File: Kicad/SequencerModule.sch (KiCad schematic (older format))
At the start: 0 parts

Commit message: added symbols on schematics
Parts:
- added A1: Arduino_Nano_v3.x, Module:Arduino_Nano, symbol MCU_Module:Arduino_Nano_v3.x
- added C1: 0.1μF, symbol Device:C_Small
- added C2, C3: 10uF, symbol Device:CP1_Small
- added C4: 0.1uF, symbol Device:C_Small
- added D1, D4: LED, symbol Device:LED
- added D2, D3: D_Small, symbol Device:D_Small
- added J1, J2, J3, J4, J5, J6, J7: TRIG_OUT, Connector_Audio:Jack_3.5mm_QingPu_WQP-PJ398SM_Vertical_CircularHoles, symbol Connector:AudioJack2_SwitchT
- added JP1: EURO_PWR_2x5, symbol eurorack_custom:urorack_EURO_PWR_2x5
- added L1, L2: L_Small, symbol Device:L_Small
- added Q1, Q2: 2N3904, Package_TO_SOT_THT:TO-92_Inline, symbol Transistor_BJT:2N3904
- added R1, R5: 1k, symbol Device:R
- added R2, R6: R1k, symbol Device:R
- added R3, R7: 1k8, symbol Device:R
- added R4, R8: 120, symbol Device:R
- added U1: L78L05_SOT89, Package_TO_SOT_SMD:SOT-89-3, symbol Regulator_Linear:L78L05_SOT89
- added U2: MCP4822, symbol Analog_DAC:MCP4822
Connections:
- net labels added: +12V, +5V, -12V, CS, DAC_CV1, DAC_CV2, GND, MCU_TRIG_OUT_1, MCU_TRIG_OUT_2, SCLK, SDI
- wire segments 0 -> 81

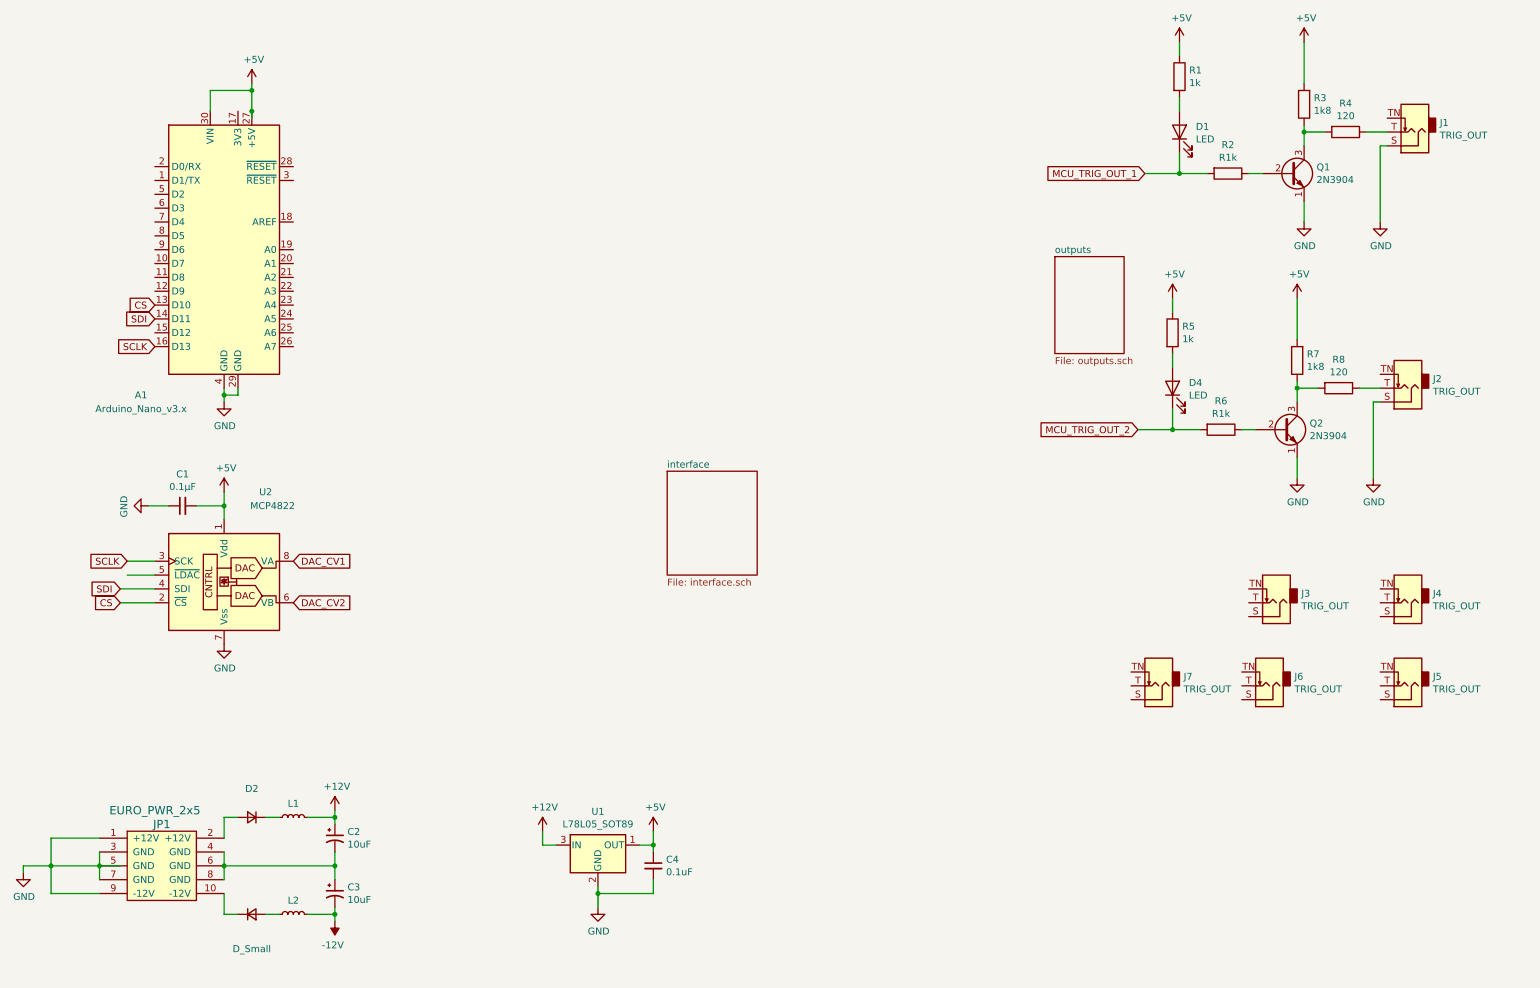
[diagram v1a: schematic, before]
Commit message: added CV output buffers
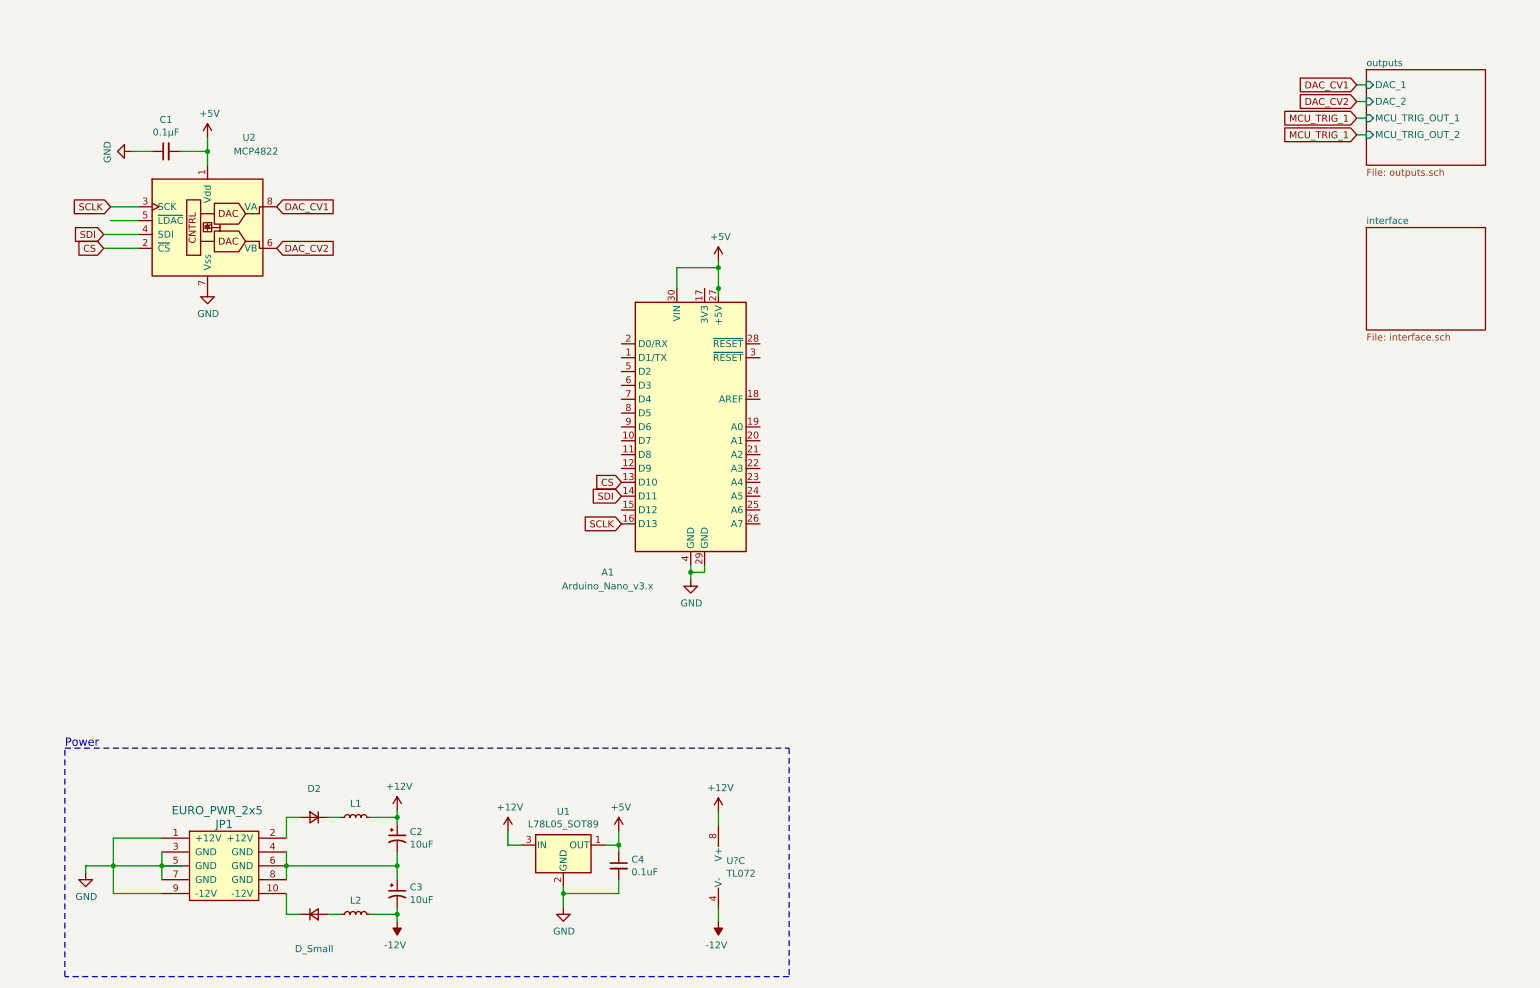
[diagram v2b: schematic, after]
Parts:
- removed D1, D4: LED, symbol Device:LED
- removed J1, J2, J3, J4, J5, J6, J7: TRIG_OUT, Connector_Audio:Jack_3.5mm_QingPu_WQP-PJ398SM_Vertical_CircularHoles, symbol Connector:AudioJack2_SwitchT
- removed Q1, Q2: 2N3904, Package_TO_SOT_THT:TO-92_Inline, symbol Transistor_BJT:2N3904
- removed R1, R5: 1k, symbol Device:R
- removed R2, R6: R1k, symbol Device:R
- removed R3, R7: 1k8, symbol Device:R
- removed R4, R8: 120, symbol Device:R
- added U?: TL072, symbol Amplifier_Operational:TL072
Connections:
- net labels added: MCU_TRIG_1
- net labels removed: MCU_TRIG_OUT_1, MCU_TRIG_OUT_2
- wire segments 81 -> 59
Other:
- note added: "Power"
- moved on the sheet: A1, C1, C2, C3, C4, D2, JP1, L1, L2, U1, U2

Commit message: making progress on interface
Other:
- moved on the sheet: A1, C1, U2
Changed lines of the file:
@@
 L Analog_DAC:MCP4822 U2
 U 1 1 5FAC40C6
-P 1880 2090
-F 0 "U2" H 2180 2690 50  0000 C CNN
-F 1 "MCP4822" H 2230 2590 50  0000 C CNN
-F 2 "" H 2680 1790 50  0001 C CNN
-F 3 "http://ww1.microchip.com/downloads/en/DeviceDoc/20002249B.pdf" H 2680 1790 50  0001 C CNN
-	1    1880 2090
+P 2790 2940
+F 0 "U2" H 3090 3540 50  0000 C CNN
+F 1 "MCP4822" H 3140 3440 50  0000 C CNN
+F 2 "" H 3590 2640 50  0001 C CNN
+F 3 "http://ww1.microchip.com/downloads/en/DeviceDoc/20002249B.pdf" H 3590 2640 50  0001 C CNN
+	1    2790 2940
 	1    0    0    -1
 $EndComp
@@
 L power:GND #PWR0101
 U 1 1 5FAC5967
-P 1880 2590
-F 0 "#PWR0101" H 1880 2340 50  0001 C CNN
-F 1 "GND" H 1885 2417 50  0000 C CNN
-F 2 "" H 1880 2590 50  0001 C CNN
-F 3 "" H 1880 2590 50  0001 C CNN
-	1    1880 2590
+P 2790 3440
+F 0 "#PWR0101" H 2790 3190 50  0001 C CNN
+F 1 "GND" H 2795 3267 50  0000 C CNN
+F 2 "" H 2790 3440 50  0001 C CNN
+F 3 "" H 2790 3440 50  0001 C CNN
+	1    2790 3440
 	1    0    0    -1
 $EndComp
@@
 L Device:C_Small C1
 U 1 1 5FAC8AF5
-P 1580 1590
-F 0 "C1" V 1809 1590 50  0000 C CNN
-F 1 "0.1μF" V 1718 1590 50  0000 C CNN
-F 2 "" H 1580 1590 50  0001 C CNN
-F 3 "~" H 1580 1590 50  0001 C CNN
-	1    1580 1590
+P 2490 2440
+F 0 "C1" V 2719 2440 50  0000 C CNN
+F 1 "0.1μF" V 2628 2440 50  0000 C CNN
+F 2 "" H 2490 2440 50  0001 C CNN
+F 3 "~" H 2490 2440 50  0001 C CNN
+	1    2490 2440
 	0    -1   -1   0
 $EndComp
 Wire Wire Line
-	1880 1490 1880 1590
-Wire Wire Line
-	1680 1590 1880 1590
-Connection ~ 1880 1590
-Wire Wire Line
-	1880 1590 1880 1690
+	2790 2340 2790 2440
+Wire Wire Line
+	2590 2440 2790 2440
+Connection ~ 2790 2440
+Wire Wire Line
+	2790 2440 2790 2540
 $Comp
 L power:GND #PWR0102
 U 1 1 5FAC9D1B
-P 1330 1590
-F 0 "#PWR0102" H 1330 1340 50  0001 C CNN
-F 1 "GND" H 1335 1417 50  0000 C CNN
-F 2 "" H 1330 1590 50  0001 C CNN
-F 3 "" H 1330 1590 50  0001 C CNN
-	1    1330 1590
+P 2240 2440
+F 0 "#PWR0102" H 2240 2190 50  0001 C CNN
+F 1 "GND" H 2245 2267 50  0000 C CNN
+F 2 "" H 2240 2440 50  0001 C CNN
+F 3 "" H 2240 2440 50  0001 C CNN
+	1    2240 2440
 	0    1    1    0
 $EndComp
 Wire Wire Line
-	1330 1590 1480 1590
-Text GLabel 1180 1990 0    50   Input ~ 0
+	2240 2440 2390 2440
+Text GLabel 2090 2840 0    50   Input ~ 0
 SCLK
-Text GLabel 1130 2290 0    50   Input ~ 0
+Text GLabel 2040 3140 0    50   Input ~ 0
 CS
-Text GLabel 2380 1990 2    50   Input ~ 0
+Text GLabel 3290 2840 2    50   Input ~ 0
 DAC_CV1
-Text GLabel 2380 2290 2    50   Input ~ 0
+Text GLabel 3290 3140 2    50   Input ~ 0
 DAC_CV2
 Wire Wire Line
-	1180 1990 1380 1990
-Wire Wire Line
-	1180 2090 1380 2090
-Wire Wire Line
-	1130 2190 1380 2190
-Wire Wire Line
-	1130 2290 1380 2290
+	2090 2840 2290 2840
+Wire Wire Line
+	2090 2940 2290 2940
+Wire Wire Line
+	2040 3040 2290 3040
+Wire Wire Line
+	2040 3140 2290 3140
 $Comp
 L MCU_Module:Arduino_Nano_v3.x A1
 U 1 1 5FAD0791
-P 5370 3580
-F 0 "A1" H 4770 2530 50  0000 C CNN
-F 1 "Arduino_Nano_v3.x" H 4770 2430 50  0000 C CNN
-F 2 "Module:Arduino_Nano" H 5370 3580 50  0001 C CIN
-F 3 "http://www.mouser.com/pdfdocs/Gravitech_Arduino_Nano3_0.pdf" H 5370 3580 50  0001 C CNN
-	1    5370 3580
+P 6920 3010
+F 0 "A1" H 6320 1960 50  0000 C CNN
+F 1 "Arduino_Nano_v3.x" H 6320 1860 50  0000 C CNN
+F 2 "Module:Arduino_Nano" H 6920 3010 50  0001 C CIN
+F 3 "http://www.mouser.com/pdfdocs/Gravitech_Arduino_Nano3_0.pdf" H 6920 3010 50  0001 C CNN
+	1    6920 3010
 	1    0    0    -1
 $EndComp
@@
 L power:GND #PWR0103
 U 1 1 5FAD2D29
-P 5370 4680
-F 0 "#PWR0103" H 5370 4430 50  0001 C CNN
-F 1 "GND" H 5375 4507 50  0000 C CNN
-F 2 "" H 5370 4680 50  0001 C CNN
-F 3 "" H 5370 4680 50  0001 C CNN
-	1    5370 4680
-	1    0    0    -1
-$EndComp
-Wire Wire Line
-	5370 4580 5370 4630
-Wire Wire Line
-	5470 4580 5470 4630
-Wire Wire Line
-	5470 4630 5370 4630
-Connection ~ 5370 4630
-Wire Wire Line
-	5370 4630 5370 4680
-Text GLabel 4870 4080 0    50   Input ~ 0
+P 6920 4110
+F 0 "#PWR0103" H 6920 3860 50  0001 C CNN
+F 1 "GND" H 6925 3937 50  0000 C CNN
+F 2 "" H 6920 4110 50  0001 C CNN
+F 3 "" H 6920 4110 50  0001 C CNN
+	1    6920 4110
+	1    0    0    -1
+$EndComp
+Wire Wire Line
+	6920 4010 6920 4060
+Wire Wire Line
+	7020 4010 7020 4060
+Wire Wire Line
+	7020 4060 6920 4060
+Connection ~ 6920 4060
+Wire Wire Line
+	6920 4060 6920 4110
+Text GLabel 6420 3510 0    50   Input ~ 0
 SDI
-Text GLabel 1130 2190 0    50   Input ~ 0
+Text GLabel 2040 3040 0    50   Input ~ 0
 SDI
-Text GLabel 4870 4280 0    50   Input ~ 0
+Text GLabel 6420 3710 0    50   Input ~ 0
 SCLK
 $Comp
@@
 L power:+5V #PWR0110
 U 1 1 5FB4B6EF
-P 1880 1490
-F 0 "#PWR0110" H 1880 1340 50  0001 C CNN
-F 1 "+5V" H 1895 1663 50  0000 C CNN
-F 2 "" H 1880 1490 50  0001 C CNN
-F 3 "" H 1880 1490 50  0001 C CNN
-	1    1880 1490
+P 2790 2340
+F 0 "#PWR0110" H 2790 2190 50  0001 C CNN
+F 1 "+5V" H 2805 2513 50  0000 C CNN
+F 2 "" H 2790 2340 50  0001 C CNN
+F 3 "" H 2790 2340 50  0001 C CNN
+	1    2790 2340
 	1    0    0    -1
 $EndComp
@@
 L power:+5V #PWR0113
 U 1 1 5FB529CE
-P 5570 2380
-F 0 "#PWR0113" H 5570 2230 50  0001 C CNN
-F 1 "+5V" H 5585 2553 50  0000 C CNN
-F 2 "" H 5570 2380 50  0001 C CNN
-F 3 "" H 5570 2380 50  0001 C CNN
-	1    5570 2380
-	1    0    0    -1
-$EndComp
-Wire Wire Line
-	5570 2630 5570 2580
-Wire Wire Line
-	5570 2380 5570 2430
-Connection ~ 5570 2580
-Wire Wire Line
-	5270 2580 5270 2430
-Wire Wire Line
-	5270 2430 5570 2430
-Connection ~ 5570 2430
-Wire Wire Line
-	5570 2430 5570 2580
-Text GLabel 4870 3980 0    50   Input ~ 0
+P 7120 1810
+F 0 "#PWR0113" H 7120 1660 50  0001 C CNN
+F 1 "+5V" H 7135 1983 50  0000 C CNN
+F 2 "" H 7120 1810 50  0001 C CNN
+F 3 "" H 7120 1810 50  0001 C CNN
+	1    7120 1810
+	1    0    0    -1
+$EndComp
+Wire Wire Line
+	7120 2060 7120 2010
+Wire Wire Line
+	7120 1810 7120 1860
+Connection ~ 7120 2010
+Wire Wire Line
+	6820 2010 6820 1860
+Wire Wire Line
+	6820 1860 7120 1860
+Connection ~ 7120 1860
+Wire Wire Line
+	7120 1860 7120 2010
+Text GLabel 6420 3410 0    50   Input ~ 0
 CS
 $Comp

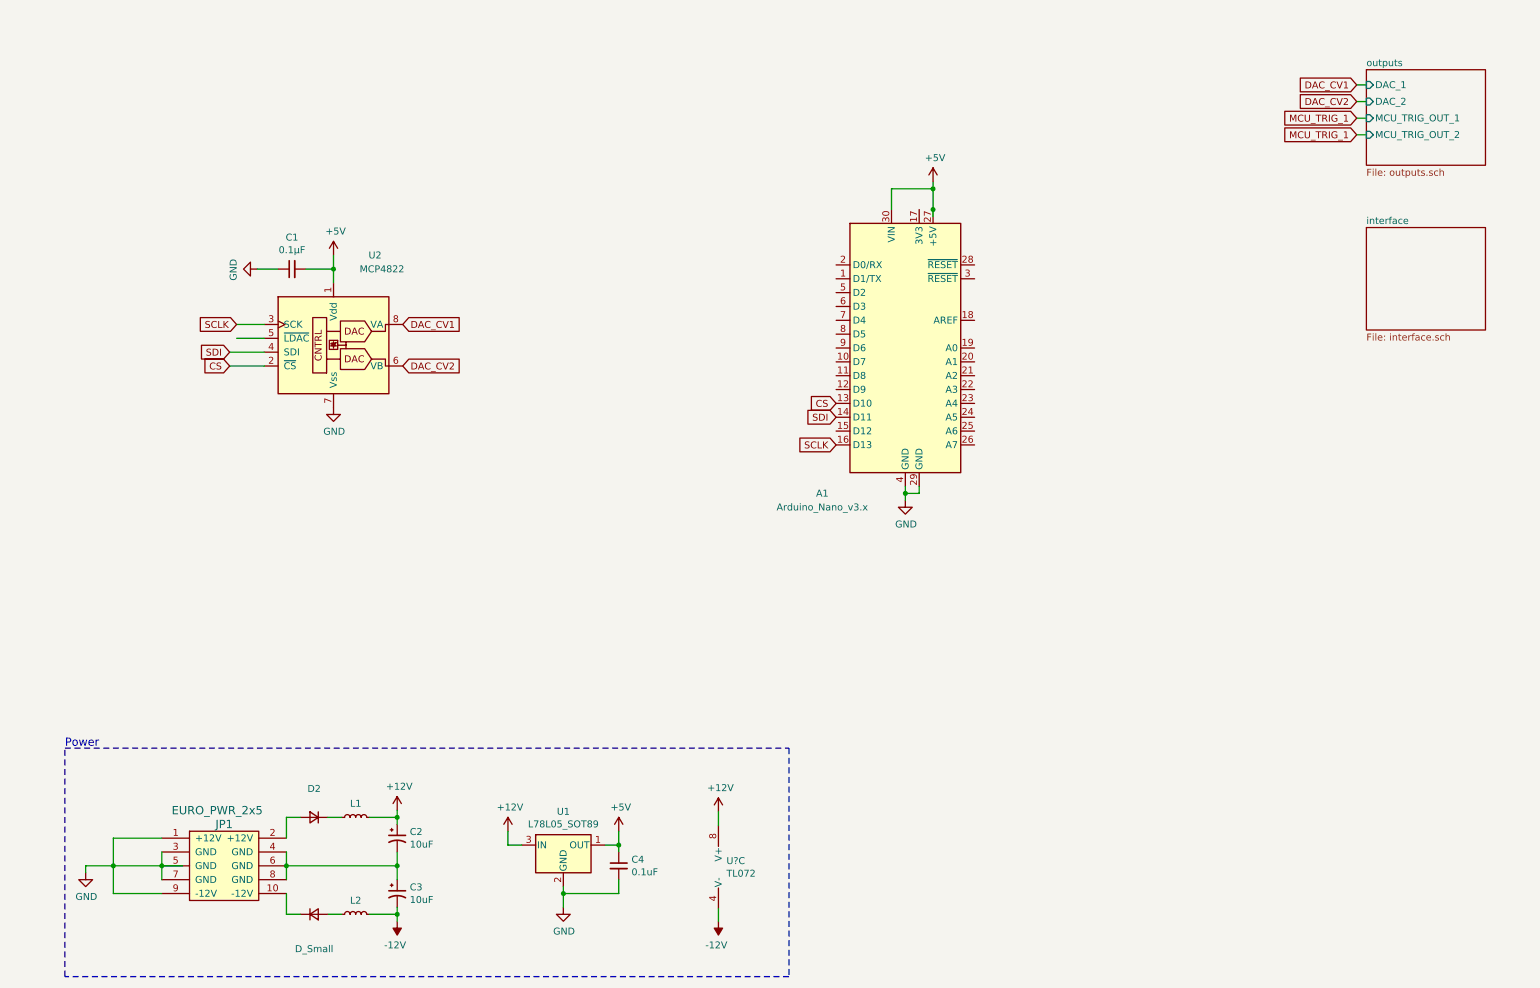
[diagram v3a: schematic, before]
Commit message: completing schematics and starting to correct errors
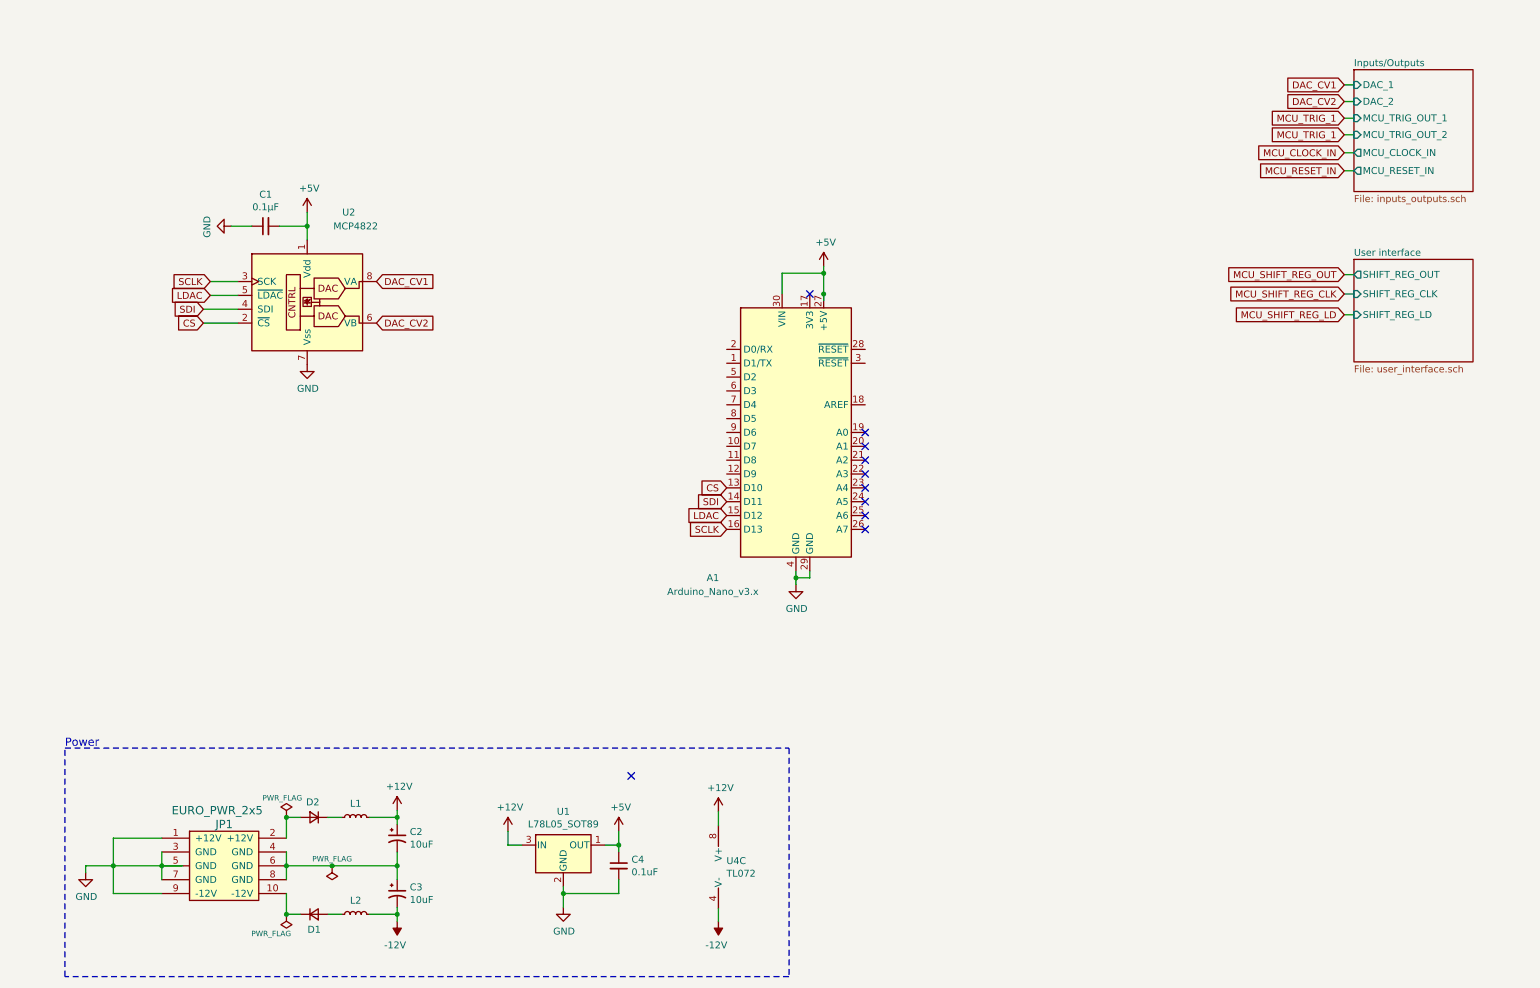
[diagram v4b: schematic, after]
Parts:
- gave numbers to parts that had none: 1
- renumbered D3 to D1
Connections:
- net labels added: LDAC, MCU_CLOCK_IN, MCU_RESET_IN, MCU_SHIFT_REG_CLK, MCU_SHIFT_REG_LD, MCU_SHIFT_REG_OUT
- wire segments 59 -> 65
- no-connect marks 0 -> 10
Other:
- moved on the sheet: A1, C1, U2
